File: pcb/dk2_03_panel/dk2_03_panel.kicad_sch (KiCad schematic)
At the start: 55 parts

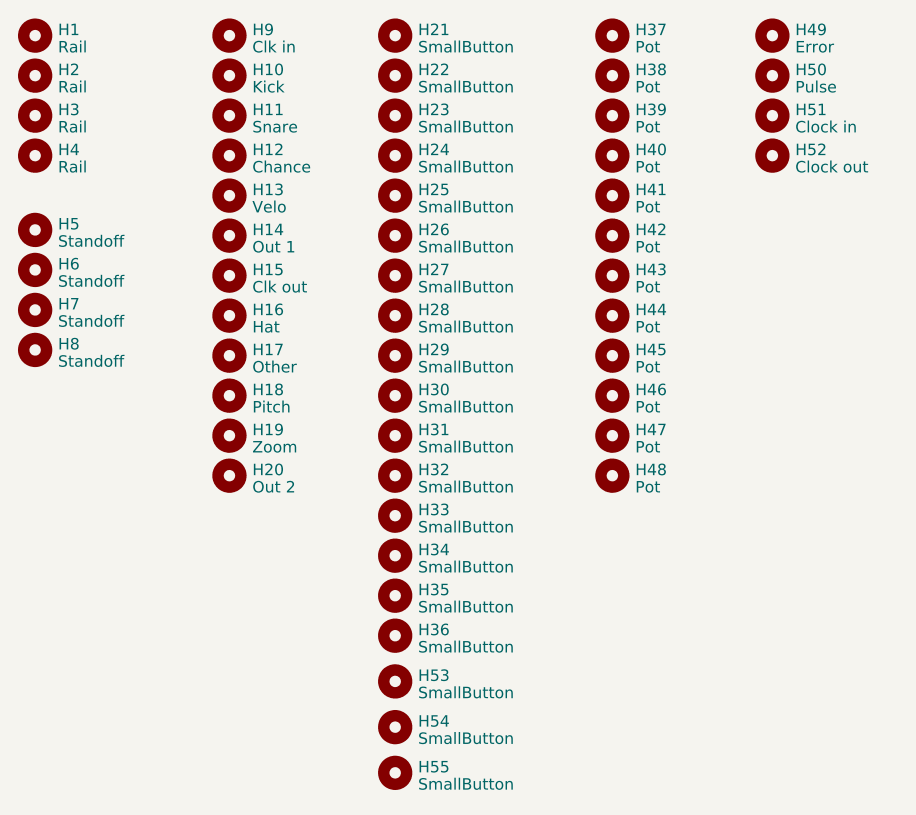
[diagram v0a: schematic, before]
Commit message: fixed an issue where i forgot to rotate the pots on the pcb
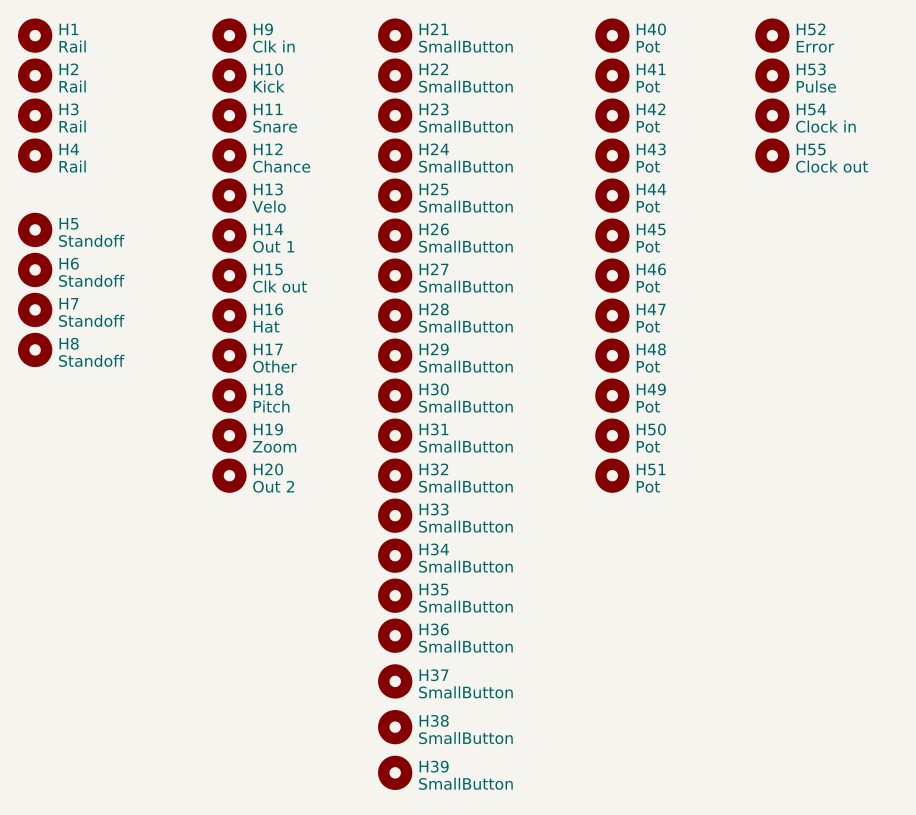
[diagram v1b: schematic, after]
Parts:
- H21, H22, H23, H24, H25, H26, H27, H28, H29, H30, H31, H32, H33, H34, H35, H36: footprint Panel:MountingHole_4.3mm_M4 -> Panel:Button_Hole
- H37: renamed from H53; footprint Panel:MountingHole_4.3mm_M4 -> Panel:Button_Hole
- H38: renamed from H54; footprint Panel:MountingHole_4.3mm_M4 -> Panel:Button_Hole
- H39: renamed from H55; footprint Panel:MountingHole_4.3mm_M4 -> Panel:Button_Hole
- H40: renamed from H37; footprint Panel:MountingHole_6.4mm_M6 -> Panel:Pot_Hole
- H41: renamed from H38; footprint Panel:MountingHole_6.4mm_M6 -> Panel:Pot_Hole
- H42: renamed from H39; footprint Panel:MountingHole_6.4mm_M6 -> Panel:Pot_Hole
- H43: renamed from H40; footprint Panel:MountingHole_6.4mm_M6 -> Panel:Pot_Hole
- H44: renamed from H41; footprint Panel:MountingHole_6.4mm_M6 -> Panel:Pot_Hole
- H45: renamed from H42; footprint Panel:MountingHole_6.4mm_M6 -> Panel:Pot_Hole
- H46: renamed from H43; footprint Panel:MountingHole_6.4mm_M6 -> Panel:Pot_Hole
- H47: renamed from H44; footprint Panel:MountingHole_6.4mm_M6 -> Panel:Pot_Hole
- H48: renamed from H45; footprint Panel:MountingHole_6.4mm_M6 -> Panel:Pot_Hole
- H49: renamed from H46; footprint Panel:MountingHole_6.4mm_M6 -> Panel:Pot_Hole
- H50: renamed from H47; footprint Panel:MountingHole_6.4mm_M6 -> Panel:Pot_Hole
- H51: renamed from H48; footprint Panel:MountingHole_6.4mm_M6 -> Panel:Pot_Hole
- renumbered H49 to H52, H50 to H53, H51 to H54, H52 to H55

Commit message: panel nearly done
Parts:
- H15: value Clk out -> Clock
- H21: value SmallButton -> Play
- H22: value SmallButton -> Tap
- H23: value SmallButton -> Live
- H24: value SmallButton -> Step
- H25: value SmallButton -> X
- H26: value SmallButton -> Save
- H27: value SmallButton -> Beat
- H28: value SmallButton -> Tempo
- H29: value SmallButton -> Tuplet
- H30: value SmallButton -> Y
- H31: value SmallButton -> Menu
- H32: value SmallButton -> Kit
- H33: value SmallButton -> T sig
- H34: value SmallButton -> Clear
- H35: value SmallButton -> Back
- H36: value SmallButton -> +
- H37: value SmallButton -> -
- H38: value SmallButton -> Yes
- H39: value SmallButton -> No
- H40: value Pot -> Chance
- H41: value Pot -> Zoom
- H42: value Pot -> Cluster
- H43: value Pot -> Crop
- H44: value Pot -> Crush
- H45: value Pot -> Pitch
- H46: value Pot -> Vel
- H47: value Pot -> Vel range
- H48: value Pot -> Magnet
- H49: value Pot -> Swing
- H50: value Pot -> Drop rand
- H51: value Pot -> Drop all
- H9: value Clk in -> Clock
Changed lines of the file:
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@@
       (effects (font (size 1.27 1.27)) (justify left))
     )
-    (property "Value" "Pot" (at 107.95 36.8373 0)
+    (property "Value" "Zoom" (at 107.95 36.8373 0)
       (effects (font (size 1.27 1.27)) (justify left))
     )
@@
       (effects (font (size 1.27 1.27)) (justify left))
     )
-    (property "Value" "SmallButton" (at 83.82 90.1773 0)
+    (property "Value" "Clear" (at 83.82 90.1773 0)
       (effects (font (size 1.27 1.27)) (justify left))
     )
@@
       (effects (font (size 1.27 1.27)) (justify left))
     )
-    (property "Value" "SmallButton" (at 83.82 41.2823 0)
+    (property "Value" "Live" (at 83.82 41.2823 0)
       (effects (font (size 1.27 1.27)) (justify left))
     )
@@
       (effects (font (size 1.27 1.27)) (justify left))
     )
-    (property "Value" "SmallButton" (at 83.82 94.6223 0)
+    (property "Value" "Back" (at 83.82 94.6223 0)
       (effects (font (size 1.27 1.27)) (justify left))
     )
@@
       (effects (font (size 1.27 1.27)) (justify left))
     )
-    (property "Value" "Pot" (at 107.95 81.2873 0)
+    (property "Value" "Drop all" (at 107.95 81.2873 0)
       (effects (font (size 1.27 1.27)) (justify left))
     )
@@
       (effects (font (size 1.27 1.27)) (justify left))
     )
-    (property "Value" "SmallButton" (at 83.82 50.1723 0)
+    (property "Value" "X" (at 83.82 50.1723 0)
       (effects (font (size 1.27 1.27)) (justify left))
     )
@@
       (effects (font (size 1.27 1.27)) (justify left))
     )
-    (property "Value" "SmallButton" (at 83.82 81.2873 0)
+    (property "Value" "Kit" (at 83.82 81.2873 0)
       (effects (font (size 1.27 1.27)) (justify left))
     )
@@
       (effects (font (size 1.27 1.27)) (justify left))
     )
-    (property "Value" "Pot" (at 107.95 63.5073 0)
+    (property "Value" "Vel range" (at 107.95 63.5073 0)
       (effects (font (size 1.27 1.27)) (justify left))
     )
@@
       (effects (font (size 1.27 1.27)) (justify left))
     )
-    (property "Value" "SmallButton" (at 83.82 36.8373 0)
+    (property "Value" "Tap" (at 83.82 36.8373 0)
       (effects (font (size 1.27 1.27)) (justify left))
     )
@@
       (effects (font (size 1.27 1.27)) (justify left))
     )
-    (property "Value" "SmallButton" (at 83.82 45.7273 0)
+    (property "Value" "Step" (at 83.82 45.7273 0)
       (effects (font (size 1.27 1.27)) (justify left))
     )
@@
       (effects (font (size 1.27 1.27)) (justify left))
     )
-    (property "Value" "SmallButton" (at 83.82 114.3073 0)
+    (property "Value" "No" (at 83.82 114.3073 0)
       (effects (font (size 1.27 1.27)) (justify left))
     )
@@
       (effects (font (size 1.27 1.27)) (justify left))
     )
-    (property "Value" "SmallButton" (at 83.82 99.0673 0)
+    (property "Value" "+" (at 83.82 99.0673 0)
       (effects (font (size 1.27 1.27)) (justify left))
     )
@@
       (effects (font (size 1.27 1.27)) (justify left))
     )
-    (property "Value" "SmallButton" (at 83.82 76.8423 0)
+    (property "Value" "Menu" (at 83.82 76.8423 0)
       (effects (font (size 1.27 1.27)) (justify left))
     )
@@
       (effects (font (size 1.27 1.27)) (justify left))
     )
-    (property "Value" "SmallButton" (at 83.82 63.5073 0)
+    (property "Value" "Tempo" (at 83.82 63.5073 0)
       (effects (font (size 1.27 1.27)) (justify left))
     )
@@
       (effects (font (size 1.27 1.27)) (justify left))
     )
-    (property "Value" "Pot" (at 107.95 59.0623 0)
+    (property "Value" "Vel" (at 107.95 59.0623 0)
       (effects (font (size 1.27 1.27)) (justify left))
     )
@@
       (effects (font (size 1.27 1.27)) (justify left))
     )
-    (property "Value" "Pot" (at 107.95 50.1723 0)
+    (property "Value" "Crush" (at 107.95 50.1723 0)
       (effects (font (size 1.27 1.27)) (justify left))
     )
@@
       (effects (font (size 1.27 1.27)) (justify left))
     )
-    (property "Value" "SmallButton" (at 83.82 59.0623 0)
+    (property "Value" "Beat" (at 83.82 59.0623 0)
       (effects (font (size 1.27 1.27)) (justify left))
     )
@@
       (effects (font (size 1.27 1.27)) (justify left))
     )
-    (property "Value" "Pot" (at 107.95 32.3923 0)
+    (property "Value" "Chance" (at 107.95 32.3923 0)
       (effects (font (size 1.27 1.27)) (justify left))
     )
@@
       (effects (font (size 1.27 1.27)) (justify left))
     )
-    (property "Value" "Clk in" (at 65.405 32.3923 0)
+    (property "Value" "Clock" (at 65.405 32.3923 0)
       (effects (font (size 1.27 1.27)) (justify left))
     )
@@
       (effects (font (size 1.27 1.27)) (justify left))
     )
-    (property "Value" "SmallButton" (at 83.82 67.9523 0)
+    (property "Value" "Tuplet" (at 83.82 67.9523 0)
       (effects (font (size 1.27 1.27)) (justify left))
     )
@@
       (effects (font (size 1.27 1.27)) (justify left))
     )
-    (property "Value" "Pot" (at 107.95 45.7273 0)
+    (property "Value" "Crop" (at 107.95 45.7273 0)
       (effects (font (size 1.27 1.27)) (justify left))
     )
@@
       (effects (font (size 1.27 1.27)) (justify left))
     )
-    (property "Value" "SmallButton" (at 83.82 54.6173 0)
+    (property "Value" "Save" (at 83.82 54.6173 0)
       (effects (font (size 1.27 1.27)) (justify left))
     )
@@
       (effects (font (size 1.27 1.27)) (justify left))
     )
-    (property "Value" "Pot" (at 107.95 72.3973 0)
+    (property "Value" "Swing" (at 107.95 72.3973 0)
       (effects (font (size 1.27 1.27)) (justify left))
     )
@@
       (effects (font (size 1.27 1.27)) (justify left))
     )
-    (property "Value" "Pot" (at 107.95 54.6173 0)
+    (property "Value" "Pitch" (at 107.95 54.6173 0)
       (effects (font (size 1.27 1.27)) (justify left))
     )
@@
       (effects (font (size 1.27 1.27)) (justify left))
     )
-    (property "Value" "SmallButton" (at 83.82 72.3973 0)
+    (property "Value" "Y" (at 83.82 72.3973 0)
       (effects (font (size 1.27 1.27)) (justify left))
     )
@@
       (effects (font (size 1.27 1.27)) (justify left))
     )
-    (property "Value" "Clk out" (at 65.405 59.0623 0)
+    (property "Value" "Clock" (at 65.405 59.0623 0)
       (effects (font (size 1.27 1.27)) (justify left))
     )
@@
       (effects (font (size 1.27 1.27)) (justify left))
     )
-    (property "Value" "Pot" (at 107.95 41.2823 0)
+    (property "Value" "Cluster" (at 107.95 41.2823 0)
       (effects (font (size 1.27 1.27)) (justify left))
     )
@@
       (effects (font (size 1.27 1.27)) (justify left))
     )
-    (property "Value" "SmallButton" (at 83.82 85.7323 0)
+    (property "Value" "T sig" (at 83.82 85.7323 0)
       (effects (font (size 1.27 1.27)) (justify left))
     )
@@
       (effects (font (size 1.27 1.27)) (justify left))
     )
-    (property "Value" "SmallButton" (at 83.82 104.1473 0)
+    (property "Value" "-" (at 83.82 104.1473 0)
       (effects (font (size 1.27 1.27)) (justify left))
     )
@@
       (effects (font (size 1.27 1.27)) (justify left))
     )
-    (property "Value" "SmallButton" (at 83.82 109.2273 0)
+    (property "Value" "Yes" (at 83.82 109.2273 0)
       (effects (font (size 1.27 1.27)) (justify left))
     )
@@
       (effects (font (size 1.27 1.27)) (justify left))
     )
-    (property "Value" "Pot" (at 107.95 67.9523 0)
+    (property "Value" "Magnet" (at 107.95 67.9523 0)
       (effects (font (size 1.27 1.27)) (justify left))
     )
@@
       (effects (font (size 1.27 1.27)) (justify left))
     )
-    (property "Value" "Pot" (at 107.95 76.8423 0)
+    (property "Value" "Drop rand" (at 107.95 76.8423 0)
       (effects (font (size 1.27 1.27)) (justify left))
     )
@@
       (effects (font (size 1.27 1.27)) (justify left))
     )
-    (property "Value" "SmallButton" (at 83.82 32.3923 0)
-      (effects (font (size 1.27 1.27)) (justify left))
-    )
+    (property "Value" "Play" (at 83.82 32.3923 0)
+      (effects (font (size 1.27 1.27)) (justify left))
+    )

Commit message: panel very nearly done
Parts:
- H10, H11, H14, H15, H16, H17, H20: footprint Panel:Jack_Hole -> Panel:Output_Jack_Hole
- H12, H13, H18, H19, H9: footprint Panel:Jack_Hole -> Panel:Input_Jack_Hole
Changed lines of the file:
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@@
       (effects (font (size 1.27 1.27)) (justify left))
     )
-    (property "Footprint" "Panel:Jack_Hole" (at 62.865 44.45 0)
+    (property "Footprint" "Panel:Input_Jack_Hole" (at 62.865 44.45 0)
       (effects (font (size 1.27 1.27)) hide)
     )
@@
       (effects (font (size 1.27 1.27)) (justify left))
     )
-    (property "Footprint" "Panel:Jack_Hole" (at 62.865 62.23 0)
+    (property "Footprint" "Panel:Output_Jack_Hole" (at 62.865 62.23 0)
       (effects (font (size 1.27 1.27)) hide)
     )
@@
       (effects (font (size 1.27 1.27)) (justify left))
     )
-    (property "Footprint" "Panel:Jack_Hole" (at 62.865 53.34 0)
+    (property "Footprint" "Panel:Output_Jack_Hole" (at 62.865 53.34 0)
       (effects (font (size 1.27 1.27)) hide)
     )
@@
       (effects (font (size 1.27 1.27)) (justify left))
     )
-    (property "Footprint" "Panel:Jack_Hole" (at 62.865 31.115 0)
+    (property "Footprint" "Panel:Input_Jack_Hole" (at 62.865 31.115 0)
       (effects (font (size 1.27 1.27)) hide)
     )
@@
       (effects (font (size 1.27 1.27)) (justify left))
     )
-    (property "Footprint" "Panel:Jack_Hole" (at 62.865 80.01 0)
+    (property "Footprint" "Panel:Output_Jack_Hole" (at 62.865 80.01 0)
       (effects (font (size 1.27 1.27)) hide)
     )
@@
       (effects (font (size 1.27 1.27)) (justify left))
     )
-    (property "Footprint" "Panel:Jack_Hole" (at 62.865 71.12 0)
+    (property "Footprint" "Panel:Input_Jack_Hole" (at 62.865 71.12 0)
       (effects (font (size 1.27 1.27)) hide)
     )
@@
       (effects (font (size 1.27 1.27)) (justify left))
     )
-    (property "Footprint" "Panel:Jack_Hole" (at 62.865 40.005 0)
+    (property "Footprint" "Panel:Output_Jack_Hole" (at 62.865 40.005 0)
       (effects (font (size 1.27 1.27)) hide)
     )
@@
       (effects (font (size 1.27 1.27)) (justify left))
     )
-    (property "Footprint" "Panel:Jack_Hole" (at 62.865 35.56 0)
+    (property "Footprint" "Panel:Output_Jack_Hole" (at 62.865 35.56 0)
       (effects (font (size 1.27 1.27)) hide)
     )
@@
       (effects (font (size 1.27 1.27)) (justify left))
     )
-    (property "Footprint" "Panel:Jack_Hole" (at 62.865 75.565 0)
+    (property "Footprint" "Panel:Input_Jack_Hole" (at 62.865 75.565 0)
       (effects (font (size 1.27 1.27)) hide)
     )
@@
       (effects (font (size 1.27 1.27)) (justify left))
     )
-    (property "Footprint" "Panel:Jack_Hole" (at 62.865 57.785 0)
+    (property "Footprint" "Panel:Output_Jack_Hole" (at 62.865 57.785 0)
       (effects (font (size 1.27 1.27)) hide)
     )
@@
       (effects (font (size 1.27 1.27)) (justify left))
     )
-    (property "Footprint" "Panel:Jack_Hole" (at 62.865 66.675 0)
+    (property "Footprint" "Panel:Output_Jack_Hole" (at 62.865 66.675 0)
       (effects (font (size 1.27 1.27)) hide)
     )
@@
       (effects (font (size 1.27 1.27)) (justify left))
     )
-    (property "Footprint" "Panel:Jack_Hole" (at 62.865 48.895 0)
-      (effects (font (size 1.27 1.27)) hide)
-    )
+    (property "Footprint" "Panel:Input_Jack_Hole" (at 62.865 48.895 0)
+      (effects (font (size 1.27 1.27)) hide)
+    )

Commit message: panel finished!
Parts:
- H13: value Velo -> Vel
- H25: value X -> A
- H30: value Y -> B
- H33: value T sig -> T.sig
- H39: value No -> X
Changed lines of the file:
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@@
       (effects (font (size 1.27 1.27)) (justify left))
     )
-    (property "Value" "X" (at 83.82 50.1723 0)
+    (property "Value" "A" (at 83.82 50.1723 0)
       (effects (font (size 1.27 1.27)) (justify left))
     )
@@
       (effects (font (size 1.27 1.27)) (justify left))
     )
-    (property "Value" "No" (at 83.82 114.3073 0)
+    (property "Value" "X" (at 83.82 114.3073 0)
       (effects (font (size 1.27 1.27)) (justify left))
     )
@@
       (effects (font (size 1.27 1.27)) (justify left))
     )
-    (property "Value" "Y" (at 83.82 72.3973 0)
+    (property "Value" "B" (at 83.82 72.3973 0)
       (effects (font (size 1.27 1.27)) (justify left))
     )
@@
       (effects (font (size 1.27 1.27)) (justify left))
     )
-    (property "Value" "T sig" (at 83.82 85.7323 0)
+    (property "Value" "T.sig" (at 83.82 85.7323 0)
       (effects (font (size 1.27 1.27)) (justify left))
     )
@@
   (symbol (lib_id "Mechanical:MountingHole") (at 81.28 107.95 0) (unit 1)
     (in_bom yes) (on_board yes) (dnp no) (fields_autoplaced)
-    (property "Reference" "H38" (at 83.82 107.3063 0)
+    (property "Reference" "H38" (at 83.82 108.2668 0)
       (effects (font (size 1.27 1.27)) (justify left))
     )
@@
       (effects (font (size 1.27 1.27)) (justify left))
     )
-    (property "Value" "Velo" (at 65.405 50.1723 0)
-      (effects (font (size 1.27 1.27)) (justify left))
-    )
+    (property "Value" "Vel" (at 65.405 50.1723 0)
+      (effects (font (size 1.27 1.27)) (justify left))
+    )
